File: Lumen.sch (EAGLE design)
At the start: 33 parts, among them J1 AVR_SPI_PRG_6PTH, U1 Tiny45-20-SMT, Y1 8Mhz

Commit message: Small updates for schematic and board.
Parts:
- R6, R8: device BlueRobotics-Main:C-EUC0402 -> BlueRobotics-Main:R-US_0402-CIRCUITHUB
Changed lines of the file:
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@@
 <part name="R7" library="resistor" deviceset="R-US_" device="R1206" value="NP"/>
 <part name="GND15" library="supply1" deviceset="GND" device=""/>
-<part name="R6" library="BlueRobotics-Main" deviceset="C-EU" device="C0402" value="15K 1/5W"/>
-<part name="R8" library="BlueRobotics-Main" deviceset="C-EU" device="C0402" value="300K"/>
+<part name="R6" library="BlueRobotics-Main" deviceset="R-US_" device="0402-CIRCUITHUB" value="15K 1/5W"/>
+<part name="R8" library="BlueRobotics-Main" deviceset="R-US_" device="0402-CIRCUITHUB" value="300K"/>
 <part name="Y1" library="SparkFun" deviceset="RESONATOR" device="SMD" value="8Mhz"/>
 </parts>
@@
 <segment>
 <pinref part="GND15" gate="1" pin="GND"/>
-<wire x1="88.9" y1="45.72" x2="86.36" y2="53.34" width="0.1524" layer="91"/>
+<wire x1="88.9" y1="45.72" x2="88.9" y2="48.26" width="0.1524" layer="91"/>
 <pinref part="R8" gate="G$1" pin="1"/>
 </segment>
@@
 <pinref part="D2" gate="G$1" pin="A"/>
 <wire x1="88.9" y1="73.66" x2="93.98" y2="73.66" width="0.1524" layer="91"/>
-<wire x1="86.36" y1="81.28" x2="88.9" y2="73.66" width="0.1524" layer="91"/>
+<wire x1="88.9" y1="76.2" x2="88.9" y2="73.66" width="0.1524" layer="91"/>
 <junction x="88.9" y="73.66"/>
-<wire x1="93.98" y1="53.34" x2="88.9" y2="73.66" width="0.1524" layer="91"/>
+<wire x1="88.9" y1="58.42" x2="88.9" y2="73.66" width="0.1524" layer="91"/>
 <pinref part="R6" gate="G$1" pin="1"/>
 <pinref part="R8" gate="G$1" pin="2"/>
@@
 <net name="SIGNAL_HV" class="0">
 <segment>
-<wire x1="93.98" y1="81.28" x2="88.9" y2="91.44" width="0.1524" layer="91"/>
+<wire x1="88.9" y1="86.36" x2="88.9" y2="91.44" width="0.1524" layer="91"/>
 <wire x1="88.9" y1="91.44" x2="101.6" y2="91.44" width="0.1524" layer="91"/>
 <label x="88.9" y="91.44" size="1.778" layer="95"/>

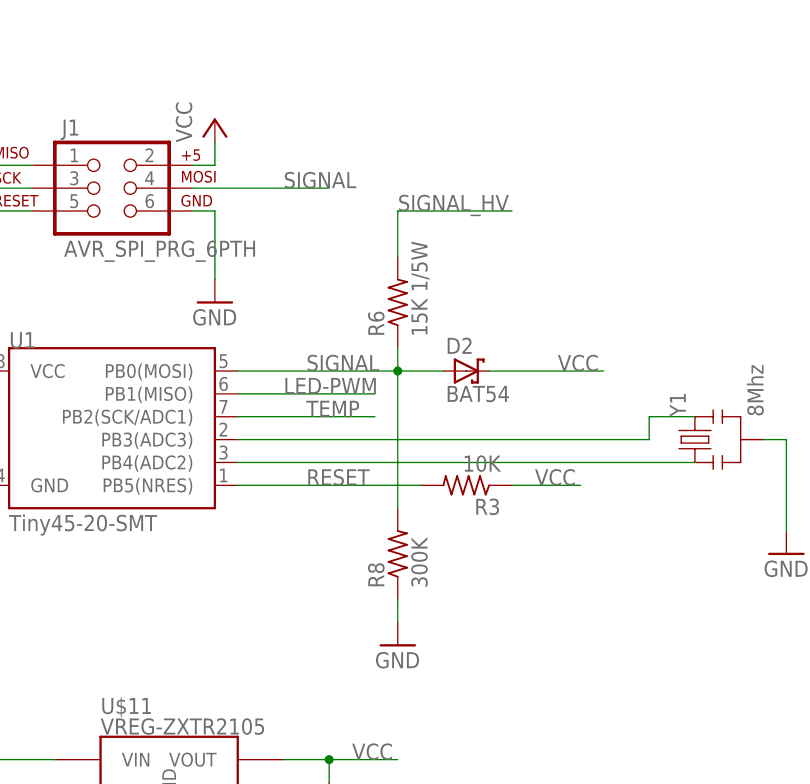
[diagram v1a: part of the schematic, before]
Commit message: Minor update to rev4 with larger solder holes for capacitor and silkscreen changes.
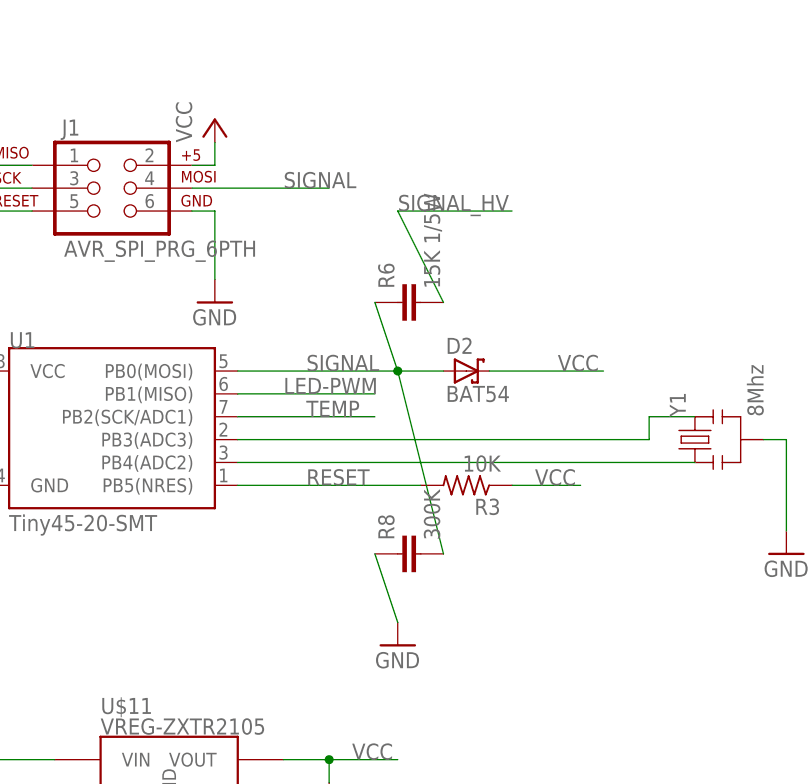
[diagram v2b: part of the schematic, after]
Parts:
- R6, R8: device BlueRobotics-Main:R-US_0402-CIRCUITHUB -> BlueRobotics-Main:CAPACITOR_0402
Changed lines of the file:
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@@
 <part name="R7" library="resistor" deviceset="R-US_" device="R1206" value="NP"/>
 <part name="GND15" library="supply1" deviceset="GND" device=""/>
-<part name="R6" library="BlueRobotics-Main" deviceset="R-US_" device="0402-CIRCUITHUB" value="15K 1/5W"/>
-<part name="R8" library="BlueRobotics-Main" deviceset="R-US_" device="0402-CIRCUITHUB" value="300K"/>
+<part name="R6" library="BlueRobotics-Main" deviceset="CAPACITOR" device="_0402" value="15K 1/5W"/>
+<part name="R8" library="BlueRobotics-Main" deviceset="CAPACITOR" device="_0402" value="300K"/>
 <part name="Y1" library="SparkFun" deviceset="RESONATOR" device="SMD" value="8Mhz"/>
 </parts>
@@
 <segment>
 <pinref part="GND15" gate="1" pin="GND"/>
-<wire x1="88.9" y1="45.72" x2="88.9" y2="48.26" width="0.1524" layer="91"/>
+<wire x1="88.9" y1="45.72" x2="86.36" y2="53.34" width="0.1524" layer="91"/>
 <pinref part="R8" gate="G$1" pin="1"/>
 </segment>
@@
 <pinref part="D2" gate="G$1" pin="A"/>
 <wire x1="88.9" y1="73.66" x2="93.98" y2="73.66" width="0.1524" layer="91"/>
-<wire x1="88.9" y1="76.2" x2="88.9" y2="73.66" width="0.1524" layer="91"/>
+<wire x1="86.36" y1="81.28" x2="88.9" y2="73.66" width="0.1524" layer="91"/>
 <junction x="88.9" y="73.66"/>
-<wire x1="88.9" y1="58.42" x2="88.9" y2="73.66" width="0.1524" layer="91"/>
+<wire x1="93.98" y1="53.34" x2="88.9" y2="73.66" width="0.1524" layer="91"/>
 <pinref part="R6" gate="G$1" pin="1"/>
 <pinref part="R8" gate="G$1" pin="2"/>
@@
 <net name="SIGNAL_HV" class="0">
 <segment>
-<wire x1="88.9" y1="86.36" x2="88.9" y2="91.44" width="0.1524" layer="91"/>
+<wire x1="93.98" y1="81.28" x2="88.9" y2="91.44" width="0.1524" layer="91"/>
 <wire x1="88.9" y1="91.44" x2="101.6" y2="91.44" width="0.1524" layer="91"/>
 <label x="88.9" y="91.44" size="1.778" layer="95"/>

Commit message: Minor layout updates for new production order.
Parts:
- R6, R8: device BlueRobotics-Main:CAPACITOR_0402 -> BlueRobotics-Main:RESISTOR_0402
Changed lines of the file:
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@@
 <part name="R7" library="resistor" deviceset="R-US_" device="R1206" value="NP"/>
 <part name="GND15" library="supply1" deviceset="GND" device=""/>
-<part name="R6" library="BlueRobotics-Main" deviceset="CAPACITOR" device="_0402" value="15K 1/5W"/>
-<part name="R8" library="BlueRobotics-Main" deviceset="CAPACITOR" device="_0402" value="300K"/>
+<part name="R6" library="BlueRobotics-Main" deviceset="RESISTOR" device="_0402" value="15K 1/5W"/>
+<part name="R8" library="BlueRobotics-Main" deviceset="RESISTOR" device="_0402" value="300K"/>
 <part name="Y1" library="SparkFun" deviceset="RESONATOR" device="SMD" value="8Mhz"/>
 </parts>
@@
 <instance part="R7" gate="G$1" x="167.64" y="142.24" rot="R270"/>
 <instance part="GND15" gate="1" x="88.9" y="43.18"/>
-<instance part="R6" gate="G$1" x="88.9" y="81.28" rot="R90"/>
+<instance part="R6" gate="G$1" x="88.9" y="81.534" rot="R90"/>
 <instance part="R8" gate="G$1" x="88.9" y="53.34" rot="R90"/>
 <instance part="Y1" gate="G$1" x="121.92" y="66.04" rot="R90"/>
@@
 <segment>
 <pinref part="GND15" gate="1" pin="GND"/>
-<wire x1="88.9" y1="45.72" x2="86.36" y2="53.34" width="0.1524" layer="91"/>
 <pinref part="R8" gate="G$1" pin="1"/>
+<wire x1="88.9" y1="48.26" x2="88.9" y2="45.72" width="0.1524" layer="91"/>
 </segment>
 </net>
@@
 <pinref part="D2" gate="G$1" pin="A"/>
 <wire x1="88.9" y1="73.66" x2="93.98" y2="73.66" width="0.1524" layer="91"/>
-<wire x1="86.36" y1="81.28" x2="88.9" y2="73.66" width="0.1524" layer="91"/>
+<wire x1="88.9" y1="76.454" x2="88.9" y2="73.66" width="0.1524" layer="91"/>
 <junction x="88.9" y="73.66"/>
-<wire x1="93.98" y1="53.34" x2="88.9" y2="73.66" width="0.1524" layer="91"/>
+<wire x1="88.9" y1="58.42" x2="88.9" y2="73.66" width="0.1524" layer="91"/>
 <pinref part="R6" gate="G$1" pin="1"/>
 <pinref part="R8" gate="G$1" pin="2"/>
@@
 <net name="SIGNAL_HV" class="0">
 <segment>
-<wire x1="93.98" y1="81.28" x2="88.9" y2="91.44" width="0.1524" layer="91"/>
+<wire x1="88.9" y1="86.614" x2="88.9" y2="91.44" width="0.1524" layer="91"/>
 <wire x1="88.9" y1="91.44" x2="101.6" y2="91.44" width="0.1524" layer="91"/>
 <label x="88.9" y="91.44" size="1.778" layer="95"/>
